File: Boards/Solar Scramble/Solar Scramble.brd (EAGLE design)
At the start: 101.6 x 63.5 mm, 18 parts

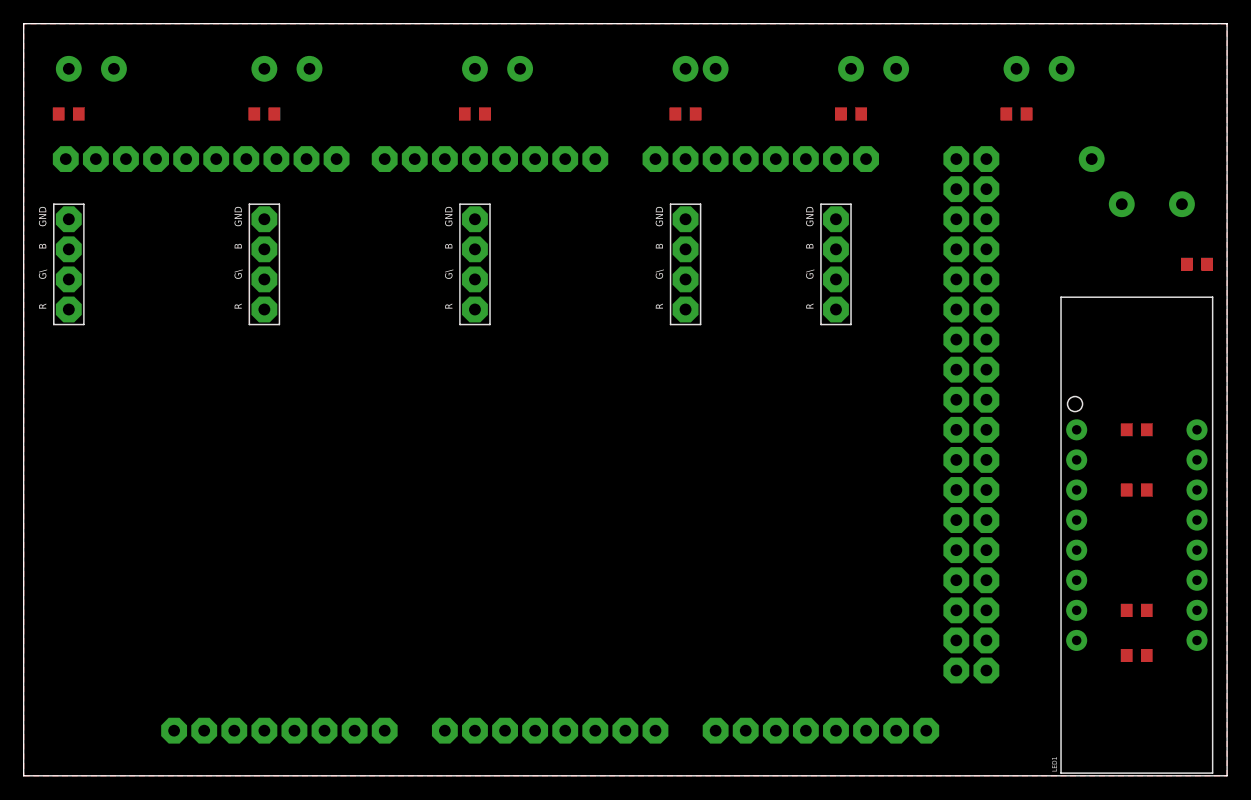
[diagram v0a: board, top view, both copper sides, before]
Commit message: Finish solar scramble
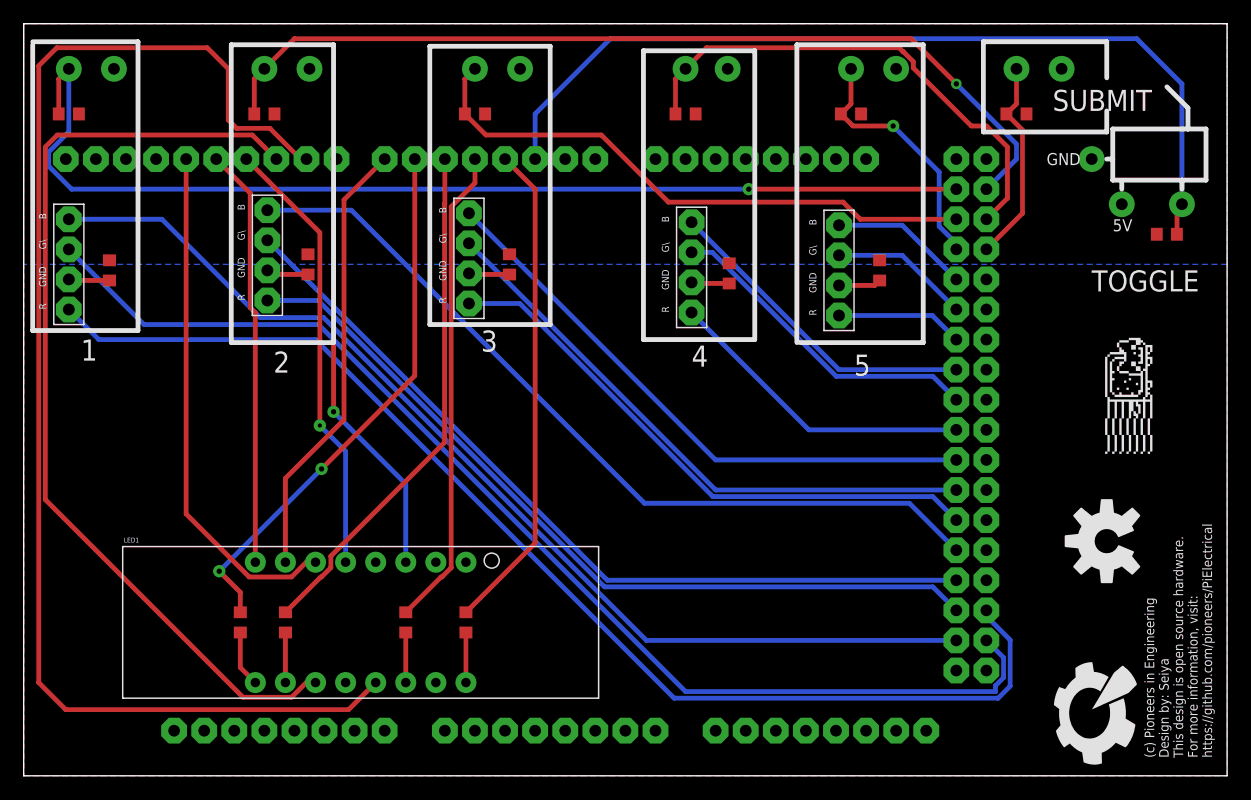
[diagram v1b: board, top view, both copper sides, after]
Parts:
- added R12, R13, R14, R15, R16: 1k, pie:R0603
- added U$7: (no value), pie:NYAN-1CM
- added U$8: (no value), pie:OSHW-LOGO-L
- added U$9: (no value), pie:PIE-LOGO-SMALL
- moved R8 75.7 mm to (18.3, 13.0), turned to 90 degrees
- moved R9 71.9 mm to (22.1, 13.0), turned to 90 degrees
- moved LED1 65.9 mm to (28.4, 13.0), turned to 0 degrees
- moved R10 62.7 mm to (32.3, 13.0), turned to 90 degrees
- moved R11 58.9 mm to (37.3, 13.0), turned to 90 degrees
- moved U$6 48.0 mm to (20.6, 43.9)
- moved U$4 18.3 mm to (56.4, 42.9)
- moved U$3 17.3 mm to (37.6, 43.7)
- moved U$5 13.0 mm to (68.8, 42.7)
- moved R7 3.59 mm to (96.5, 45.7), turned to 180 degrees
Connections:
- removed net 29: U$1.29, U$2.G
- removed net 31: U$1.31, U$6.R
- removed net 33: U$1.33, U$6.B
- removed net 35: U$1.35, U$3.G
- removed net 37: U$1.37, U$4.R
- removed net 39: U$1.39, U$4.B
- removed net 41: U$1.41, U$5.G
- new net 44: U$1.44, U$3.R
- new net 46: U$1.46, U$6.B
- new net 48: U$1.48, U$6.G
- new net 50: U$1.50, U$6.R
- new net 51: U$1.51, U$2.R
- new net 52: U$1.52, U$2.B
- new net 53: U$1.53, U$2.G
- new net N$1: R15.2, U$4.GND
- new net N$2: R12.2, U$2.GND
- new net N$7: R13.2, U$6.GND
- new net N$8: R14.2, U$3.GND
- new net N$9: R16.2, U$5.GND
- net 28: now also U$5.B; no longer U$2.R
- net 30: now also U$5.G; no longer U$2.B
- net 32: now also U$5.R; no longer U$6.G
- net 34: now also U$4.B; no longer U$3.R
- net 36: now also U$4.G; no longer U$3.B
- net 38: now also U$4.R; no longer U$4.G
- net 40: now also U$3.B; no longer U$5.R
- net 42: now also U$3.G; no longer U$5.B
- net 5V: now also U$1.5V1, U$1.5V2
- net GND: now also R12.1, R13.1, R14.1, R15.1, R16.1; no longer U$2.CAT, U$3.CAT, U$4.CAT, U$5.CAT, U$6.CAT
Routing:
- net 9: track 0.00 -> 112.1 mm
- net 51: track 0.00 -> 100.7 mm
- net 53: track 0.00 -> 98.9 mm
- net 22: track 0.00 -> 90.5 mm, vias 1 -> 2
- net 52: track 0.00 -> 89.7 mm
- net 10: track 0.00 -> 80.8 mm
- net 23: track 0.00 -> 77.3 mm, vias 1 -> 2
- net 2: track 0.00 -> 75.5 mm
- net 48: track 0.00 -> 70.1 mm
- net 46: track 0.00 -> 70.1 mm
- net 50: track 0.00 -> 69.0 mm
- net 42: track 0.00 -> 49.8 mm
- net 40: track 0.00 -> 49.8 mm
- net 24: track 0.00 -> 49.3 mm
- net 44: track 0.00 -> 48.7 mm
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- added copper zone on layer 16, net 5V
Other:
- board text added: "(c) Pioneers in Engineering Design by: Seiya This design is open source hardware. For more information, visit: https://github.com/pioneers/PiElectrical"
- board text added: "1"
- board text added: "2"
- board text added: "3"
- board text added: "4"
- board text added: "5"
- board text added: "5V"
- board text added: "GND"
- board text added: "SUBMIT"
- board text added: "TOGGLE"

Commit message: Make some changes
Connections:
- net 5V: no longer U$1.5V
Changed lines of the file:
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@@
 <drawing>
 <settings>
-<setting alwaysvectorfont="no"/>
+<setting alwaysvectorfont="yes"/>
 <setting verticaltext="up"/>
 </settings>
@@
 </signal>
 <signal name="5V">
-<contactref element="U$1" pad="5V"/>
 <via x="7.62" y="59.69" extent="1-16" drill="0.9906" diameter="2.1844"/>
 <via x="92.71" y="48.26" extent="1-16" drill="0.9906" diameter="2.1844"/>

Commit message: Finish up board
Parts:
- moved U$7 56.1 mm to (42.2, 26.4), turned to 0 degrees
- moved R7 37.3 mm to (68.3, 21.3)
- moved U$9 12.7 mm to (90.2, 18.3)
- moved U$8 12.2 mm to (90.9, 7.62)
- moved R6 0.57 mm to (83.3, 56.1), turned to 180 degrees
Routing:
- net 5V: track 0.00 -> 49.3 mm
- net 2: track 75.5 -> 45.2 mm
- net GND: track 0.00 -> 19.4 mm, vias 1 -> 2
- net 10: track 80.8 -> 93.7 mm
- net 22: track 90.5 -> 88.5 mm
- net 9: track 112.1 -> 113.0 mm
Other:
- board size 101.6 x 63.5 mm -> 95.2 x 63.5 mm
